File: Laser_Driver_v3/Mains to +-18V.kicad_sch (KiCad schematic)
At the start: 24 parts, among them Q7 Q_NMOS_DGS IRF530, Q9 Q_PMOS_DGS IRF9530, T2 Transformer_1P_SS

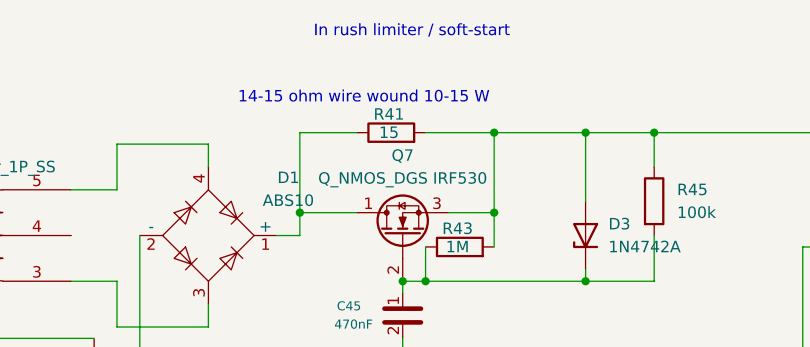
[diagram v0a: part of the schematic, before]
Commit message: More updates for the power supply
H-bridge for TEC making sense.  +/-6V supply now making sense with capacitor multiplier good for 3A per polarity.
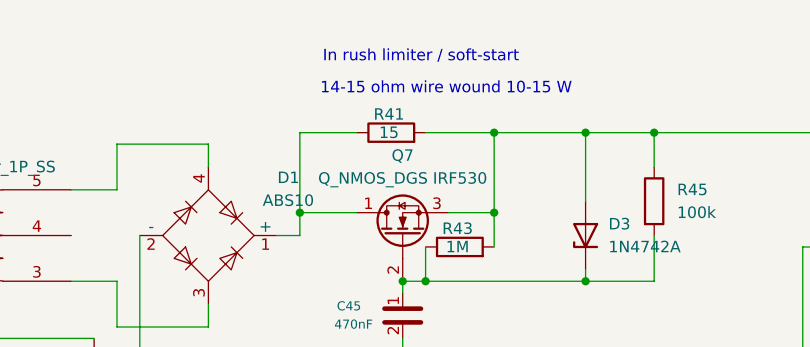
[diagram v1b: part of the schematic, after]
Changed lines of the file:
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@@
 	(text "14-15 ohm wire wound 10-15 W"
 		(exclude_from_sim no)
-		(at 130.302 48.26 0)
+		(at 139.446 47.244 0)
 		(effects
 			(font
@@
 	(text "In rush limiter / soft-start"
 		(exclude_from_sim no)
-		(at 135.636 40.894 0)
+		(at 136.652 43.688 0)
 		(effects
 			(font
@@
 	)
 	(image
-		(at 92.71 146.05)
+		(at 227.33 129.54)
 		(data "iVBORw0KGgoAAAANSUhEUgAABIwAAALOCAYAAADLFojyAAAABHNCSVQICAgIfAhkiAAAIABJREFU"
 			"eJzs3XmYFOW1P/DvqZ5eZno2hmHY930XAUFREXDDPS5o3DUmam5iEnPvTUxi0CRek5ubPT+NxiXG"

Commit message: Renumbered schematics, corrections, power verified
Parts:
- F1: renamed from F2; value 1A SlowBlow -Check current -> 1A SlowBlow
- renumbered C45 to C1, C46 to C2, C47 to C3, C48 to C4, C49 to C5, C50 to C6, C51 to C7, C52 to C8, Q7 to Q1, Q9 to Q2, R40 to R1, R41 to R2, R42 to R3, R43 to R4, R44 to R5, R45 to R6, R46 to R7, R47 to R8, R48 to R9, T2 to T1
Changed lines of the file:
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@@
 	)
 	(global_label "-18V"
-		(shape output)
+		(shape input)
 		(at 247.65 82.55 0)
 		(fields_autoplaced yes)
@@
 	)
 	(global_label "+18V"
-		(shape output)
+		(shape input)
 		(at 247.65 52.07 0)
 		(fields_autoplaced yes)
@@
 		(in_pos_files yes)
 		(dnp no)
-		(property "Reference" "R41"
+		(property "Reference" "R2"
 			(at 133.096 50.038 90)
 			(show_name no)
@@
 			(project "laser_driver_v3"
 				(path "/b2c3d4e5-f6a7-8901-bcde-f12345678901/06a154d7-731d-44d9-be1c-56d316ca362e"
-					(reference "R41")
+					(reference "R2")
 					(unit 1)
 				)
@@
 		(dnp no)
 		(fields_autoplaced yes)
-		(property "Reference" "#PWR015"
+		(property "Reference" "#PWR04"
 			(at 248.92 71.12 0)
 			(hide yes)
@@
 			(project "laser_driver_v3"
 				(path "/b2c3d4e5-f6a7-8901-bcde-f12345678901/06a154d7-731d-44d9-be1c-56d316ca362e"
-					(reference "#PWR015")
+					(reference "#PWR04")
 					(unit 1)
 				)
@@
 		(in_pos_files yes)
 		(dnp no)
-		(property "Reference" "C45"
+		(property "Reference" "C1"
 			(at 128.656 71.346 0)
 			(show_name no)
@@
 			(project "laser_driver_v3"
 				(path "/b2c3d4e5-f6a7-8901-bcde-f12345678901/06a154d7-731d-44d9-be1c-56d316ca362e"
-					(reference "C45")
+					(reference "C1")
 					(unit 1)
 				)
@@
 		(in_pos_files yes)
 		(dnp no)
-		(property "Reference" "R40"
+		(property "Reference" "R1"
 			(at 75.184 72.898 90)
 			(show_name no)
@@
 			(project "laser_driver_v3"
 				(path "/b2c3d4e5-f6a7-8901-bcde-f12345678901/06a154d7-731d-44d9-be1c-56d316ca362e"
-					(reference "R40")
+					(reference "R1")
 					(unit 1)
 				)
@@
 		(in_pos_files yes)
 		(dnp no)
-		(property "Reference" "R48"
+		(property "Reference" "R9"
 			(at 208.026 80.264 90)
 			(show_name no)
@@
 			(project "laser_driver_v3"
 				(path "/b2c3d4e5-f6a7-8901-bcde-f12345678901/06a154d7-731d-44d9-be1c-56d316ca362e"
-					(reference "R48")
+					(reference "R9")
 					(unit 1)
 				)
@@
 		(dnp no)
 		(fields_autoplaced yes)
-		(property "Reference" "Q7"
+		(property "Reference" "Q1"
 			(at 134.62 54.61 90)
 			(show_name no)
@@
 			(project "laser_driver_v3"
 				(path "/b2c3d4e5-f6a7-8901-bcde-f12345678901/06a154d7-731d-44d9-be1c-56d316ca362e"
-					(reference "Q7")
+					(reference "Q1")
 					(unit 1)
 				)
@@
 		(dnp no)
 		(fields_autoplaced yes)
-		(property "Reference" "R45"
+		(property "Reference" "R6"
 			(at 165.1 58.4199 0)
 			(show_name no)
@@
 			(project "laser_driver_v3"
 				(path "/b2c3d4e5-f6a7-8901-bcde-f12345678901/06a154d7-731d-44d9-be1c-56d316ca362e"
-					(reference "R45")
+					(reference "R6")
 					(unit 1)
 				)
@@
 		(in_pos_files yes)
 		(dnp no)
-		(property "Reference" "R47"
+		(property "Reference" "R8"
 			(at 205.486 49.53 90)
 			(show_name no)
@@
 			(project "laser_driver_v3"
 				(path "/b2c3d4e5-f6a7-8901-bcde-f12345678901/06a154d7-731d-44d9-be1c-56d316ca362e"
-					(reference "R47")
+					(reference "R8")
 					(unit 1)
 				)
@@
 		(in_pos_files yes)
 		(dnp no)
-		(property "Reference" "C52"
+		(property "Reference" "C8"
 			(at 235.336 76.426 0)
 			(show_name no)
@@
 			(project "laser_driver_v3"
 				(path "/b2c3d4e5-f6a7-8901-bcde-f12345678901/06a154d7-731d-44d9-be1c-56d316ca362e"
-					(reference "C52")
+					(reference "C8")
 					(unit 1)
 				)
@@
 		(in_pos_files yes)
 		(dnp no)
-		(property "Reference" "C46"
+		(property "Reference" "C2"
 			(at 128.656 101.826 0)
 			(show_name no)
@@
 			(project "laser_driver_v3"
 				(path "/b2c3d4e5-f6a7-8901-bcde-f12345678901/06a154d7-731d-44d9-be1c-56d316ca362e"
-					(reference "C46")
+					(reference "C2")
 					(unit 1)
 				)
@@
 		(dnp no)
 		(fields_autoplaced yes)
-		(property "Reference" "C48"
+		(property "Reference" "C4"
 			(at 195.58 72.7709 0)
 			(show_name no)
@@
 			(project "laser_driver_v3"
 				(path "/b2c3d4e5-f6a7-8901-bcde-f12345678901/06a154d7-731d-44d9-be1c-56d316ca362e"
-					(reference "C48")
+					(reference "C4")
 					(unit 1)
 				)
@@
 		(dnp no)
 		(fields_autoplaced yes)
-		(property "Reference" "C49"
+		(property "Reference" "C5"
 			(at 223.52 57.5309 0)
 			(show_name no)
@@
 			(project "laser_driver_v3"
 				(path "/b2c3d4e5-f6a7-8901-bcde-f12345678901/06a154d7-731d-44d9-be1c-56d316ca362e"
-					(reference "C49")
+					(reference "C5")
 					(unit 1)
 				)
@@
 		(in_pos_files yes)
 		(dnp no)
-		(property "Reference" "F2"
+		(property "Reference" "F1"
 			(at 68.834 55.118 90)
 			(show_name no)
@@
 			)
 		)
-		(property "Value" "1A SlowBlow -Check current"
+		(property "Value" "1A SlowBlow"
 			(at 68.58 56.642 90)
 			(show_name no)
@@
 			(project "laser_driver_v3"
 				(path "/b2c3d4e5-f6a7-8901-bcde-f12345678901/06a154d7-731d-44d9-be1c-56d316ca362e"
-					(reference "F2")
+					(reference "F1")
 					(unit 1)
 				)
@@
 		(in_pos_files yes)
 		(dnp no)
-		(property "Reference" "R42"
+		(property "Reference" "R3"
 			(at 133.096 80.518 90)
 			(show_name no)
@@
 			(project "laser_driver_v3"
 				(path "/b2c3d4e5-f6a7-8901-bcde-f12345678901/06a154d7-731d-44d9-be1c-56d316ca362e"
-					(reference "R42")
+					(reference "R3")
 					(unit 1)
 				)
@@
 		(dnp no)
 		(fields_autoplaced yes)
-		(property "Reference" "#PWR013"
+		(property "Reference" "#PWR02"
 			(at 100.33 81.28 0)
 			(hide yes)
@@
 			(project "laser_driver_v3"
 				(path "/b2c3d4e5-f6a7-8901-bcde-f12345678901/06a154d7-731d-44d9-be1c-56d316ca362e"
-					(reference "#PWR013")
+					(reference "#PWR02")
 					(unit 1)
 				)
@@
 		(dnp no)
 		(fields_autoplaced yes)
-		(property "Reference" "R46"
+		(property "Reference" "R7"
 			(at 165.1 90.1699 0)
 			(show_name no)
@@
 			(project "laser_driver_v3"
 				(path "/b2c3d4e5-f6a7-8901-bcde-f12345678901/06a154d7-731d-44d9-be1c-56d316ca362e"
-					(reference "R46")
+					(reference "R7")
 					(unit 1)
 				)
@@
 		(dnp no)
 		(fields_autoplaced yes)
-		(property "Reference" "#PWR014"
+		(property "Reference" "#PWR03"
 			(at 134.62 113.03 0)
 			(hide yes)
@@
 			(project "laser_driver_v3"
 				(path "/b2c3d4e5-f6a7-8901-bcde-f12345678901/06a154d7-731d-44d9-be1c-56d316ca362e"
-					(reference "#PWR014")
+					(reference "#PWR03")
 					(unit 1)
 				)
@@
 		(in_pos_files yes)
 		(dnp no)
-		(property "Reference" "R44"
+		(property "Reference" "R5"
 			(at 145.542 101.6 0)
 			(show_name no)
@@
 			(project "laser_driver_v3"
 				(path "/b2c3d4e5-f6a7-8901-bcde-f12345678901/06a154d7-731d-44d9-be1c-56d316ca362e"
-					(reference "R44")
+					(reference "R5")
 					(unit 1)
 				)
@@
 		(in_pos_files yes)
 		(dnp no)
-		(property "Reference" "R43"
+		(property "Reference" "R4"
 			(at 140.716 62.738 90)
 			(show_name no)
@@
 			(project "laser_driver_v3"
 				(path "/b2c3d4e5-f6a7-8901-bcde-f12345678901/06a154d7-731d-44d9-be1c-56d316ca362e"
-					(reference "R43")
+					(reference "R4")
 					(unit 1)
 				)
@@
 		(dnp no)
 		(fields_autoplaced yes)
-		(property "Reference" "C50"
+		(property "Reference" "C6"
 			(at 223.52 72.7709 0)
 			(show_name no)
@@
 			(project "laser_driver_v3"
 				(path "/b2c3d4e5-f6a7-8901-bcde-f12345678901/06a154d7-731d-44d9-be1c-56d316ca362e"
-					(reference "C50")
+					(reference "C6")
 					(unit 1)
 				)
@@
 		(dnp no)
 		(fields_autoplaced yes)
-		(property "Reference" "C47"
+		(property "Reference" "C3"
 			(at 195.58 58.8009 0)
 			(show_name no)
@@
 			(project "laser_driver_v3"
 				(path "/b2c3d4e5-f6a7-8901-bcde-f12345678901/06a154d7-731d-44d9-be1c-56d316ca362e"
-					(reference "C47")
+					(reference "C3")
 					(unit 1)
 				)
@@
 		(in_pos_files yes)
 		(dnp no)
-		(property "Reference" "C51"
+		(property "Reference" "C7"
 			(at 235.336 54.836 0)
 			(show_name no)
@@
 			(project "laser_driver_v3"
 				(path "/b2c3d4e5-f6a7-8901-bcde-f12345678901/06a154d7-731d-44d9-be1c-56d316ca362e"
-					(reference "C51")
+					(reference "C7")
 					(unit 1)
 				)
@@
 		(dnp no)
 		(fields_autoplaced yes)
-		(property "Reference" "#PWR011"
+		(property "Reference" "#PWR01"
 			(at 50.8 81.28 0)
 			(hide yes)
@@
 			(project "laser_driver_v3"
 				(path "/b2c3d4e5-f6a7-8901-bcde-f12345678901/06a154d7-731d-44d9-be1c-56d316ca362e"
-					(reference "#PWR011")
+					(reference "#PWR01")
 					(unit 1)
 				)
@@
 		(dnp no)
 		(fields_autoplaced yes)
-		(property "Reference" "T2"
+		(property "Reference" "T1"
 			(at 87.6427 53.34 0)
 			(show_name no)
@@
 			(project "laser_driver_v3"
 				(path "/b2c3d4e5-f6a7-8901-bcde-f12345678901/06a154d7-731d-44d9-be1c-56d316ca362e"
-					(reference "T2")
+					(reference "T1")
 					(unit 1)
 				)
@@
 		(dnp no)
 		(fields_autoplaced yes)
-		(property "Reference" "Q9"
+		(property "Reference" "Q2"
 			(at 134.62 85.09 90)
 			(show_name no)
@@
 			(project "laser_driver_v3"
 				(path "/b2c3d4e5-f6a7-8901-bcde-f12345678901/06a154d7-731d-44d9-be1c-56d316ca362e"
-					(reference "Q9")
-					(unit 1)
-				)
+					(reference "Q2")
+					(unit 1)
+				)
